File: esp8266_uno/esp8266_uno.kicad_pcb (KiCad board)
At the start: 2 copper layers, 69 x 53.9 mm, 131 parts, among them J1 Barrel_Jack, P1 USB, Q1 2N2222, Q2 2N2222, SW1 RESET, U1 ESP-12, U2 AMS1117-3.3, U3 CH340G, U4 ESP-13-WROOM-02, X1 12MHz

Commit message: added esp8266 in arduino uno format - hw design 5th pass
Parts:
- removed V13_13, V13_14, V14_11, V14_12, V14_13, V14_9, V15_10, V15_2, V17_5, V5_10, V5_11, V5_12, V6_4, V6_5, V7_10, V7_11: AUTO_VIA, VIA_MATRIX
- added D1: SS34, w_smd_diode:do214ab, F.Cu at (126.0, 117.0)
- added V10_11: AUTO_VIA, VIA_MATRIX, F.Cu at (141.9, 118.7)
- added V11_13: AUTO_VIA, VIA_MATRIX, F.Cu at (145.7, 126.3)
- added V18_1: AUTO_VIA, VIA_MATRIX, F.Cu at (172.4, 80.6)
- added V18_3: AUTO_VIA, VIA_MATRIX, F.Cu at (172.4, 88.2)
- added V18_4: AUTO_VIA, VIA_MATRIX, F.Cu at (172.4, 92.0)
- added V18_8: AUTO_VIA, VIA_MATRIX, F.Cu at (172.4, 107.3)
- added V18_9: AUTO_VIA, VIA_MATRIX, F.Cu at (172.4, 111.1)
- added V3_7: AUTO_VIA, VIA_MATRIX, F.Cu at (115.2, 103.5)
- added V5_1: AUTO_VIA, VIA_MATRIX, F.Cu at (122.9, 80.6)
- added V6_12: AUTO_VIA, VIA_MATRIX, F.Cu at (126.7, 122.5)
- added V9_12: AUTO_VIA, VIA_MATRIX, F.Cu at (138.1, 122.5)
- U1: footprint ESP-12 -> myfootprints:ESP-12
- moved V13_12 0.88 mm to (153.3, 122.5)
- moved V17_3 0.86 mm to (168.6, 88.2)
- moved V13_11 0.85 mm to (153.3, 118.7)
- moved V12_12 0.85 mm to (149.5, 122.5)
- moved V13_10 0.82 mm to (153.3, 114.9)
- moved V12_11 0.81 mm to (149.5, 118.7)
- moved V16_3 0.81 mm to (164.8, 88.2)
- moved V8_14 0.81 mm to (134.3, 130.1)
- moved V13_9 0.79 mm to (153.3, 111.1)
- moved V9_13 0.79 mm to (138.1, 126.3)
- moved V7_14 0.78 mm to (130.5, 130.1)
- moved V10_12 0.78 mm to (141.9, 122.5)
- moved V12_10 0.78 mm to (149.5, 114.9)
- moved V11_11 0.78 mm to (145.7, 118.7)
- moved V8_13 0.76 mm to (134.3, 126.3)
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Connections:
- A1 pad 1: Net-(A1-Pad1) -> (no net)
- A1 pad 10: Net-(A1-Pad10) -> (no net)
- A1 pad 11: Net-(A1-Pad11) -> (no net)
- A1 pad 12: Net-(A1-Pad12) -> (no net)
- A1 pad 2: Net-(A1-Pad2) -> (no net)
- A1 pad 24: Net-(A1-Pad24) -> (no net)
- A1 pad 25: Net-(A1-Pad25) -> (no net)
- A1 pad 26: Net-(A1-Pad26) -> (no net)
- A1 pad 27: Net-(A1-Pad27) -> (no net)
- A1 pad 28: Net-(A1-Pad28) -> (no net)
- A1 pad 30: Net-(A1-Pad30) -> (no net)
- A1 pad 8: Net-(A1-Pad8) -> (no net)
- J1 pad 1: +5V -> Net-(D1-Pad2)
- U3 pad 10: Net-(U3-Pad10) -> (no net)
- U3 pad 11: Net-(U3-Pad11) -> (no net)
- U3 pad 12: Net-(U3-Pad12) -> (no net)
- U3 pad 15: Net-(U3-Pad15) -> (no net)
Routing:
- net +5V: track 77.7 -> 68.6 mm
- net Net-(D1-Pad2): track 0.00 -> 8.39 mm

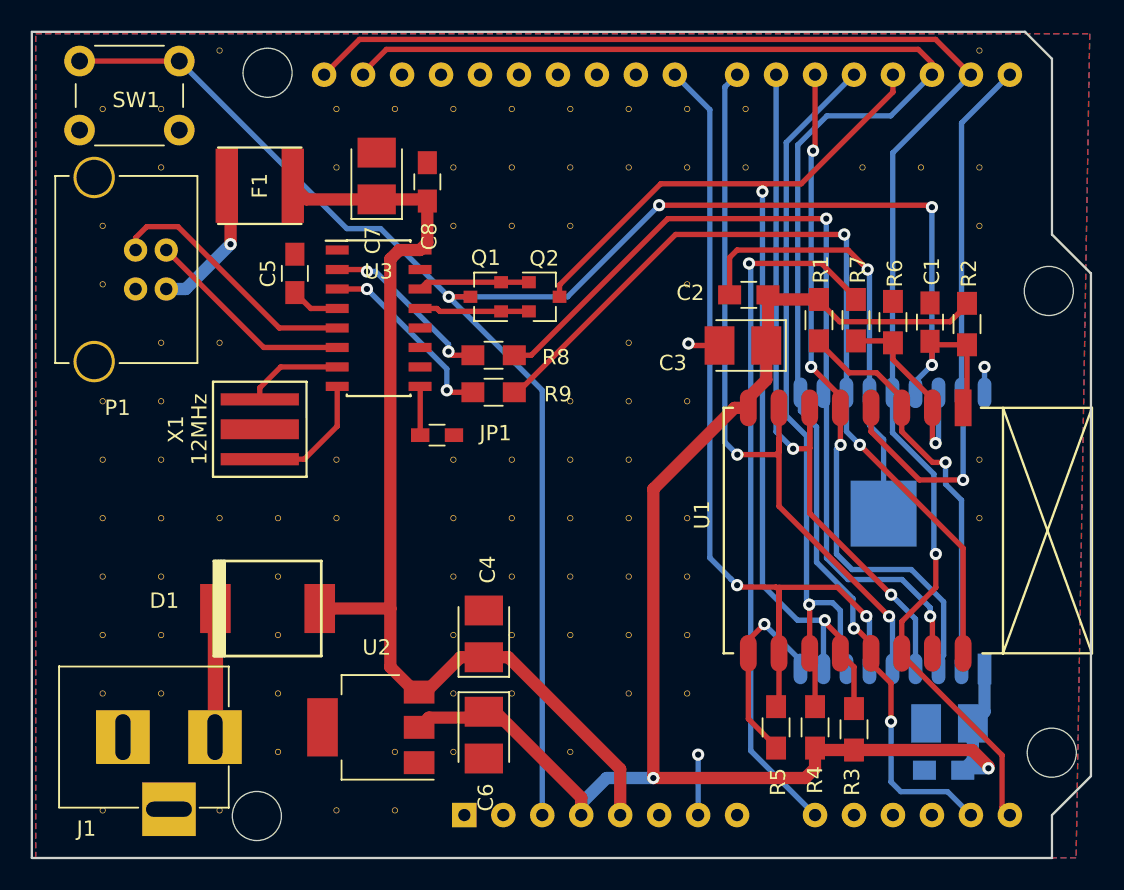
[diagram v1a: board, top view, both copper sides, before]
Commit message: added esp8266 in arduino uno format - hw design 6th pass
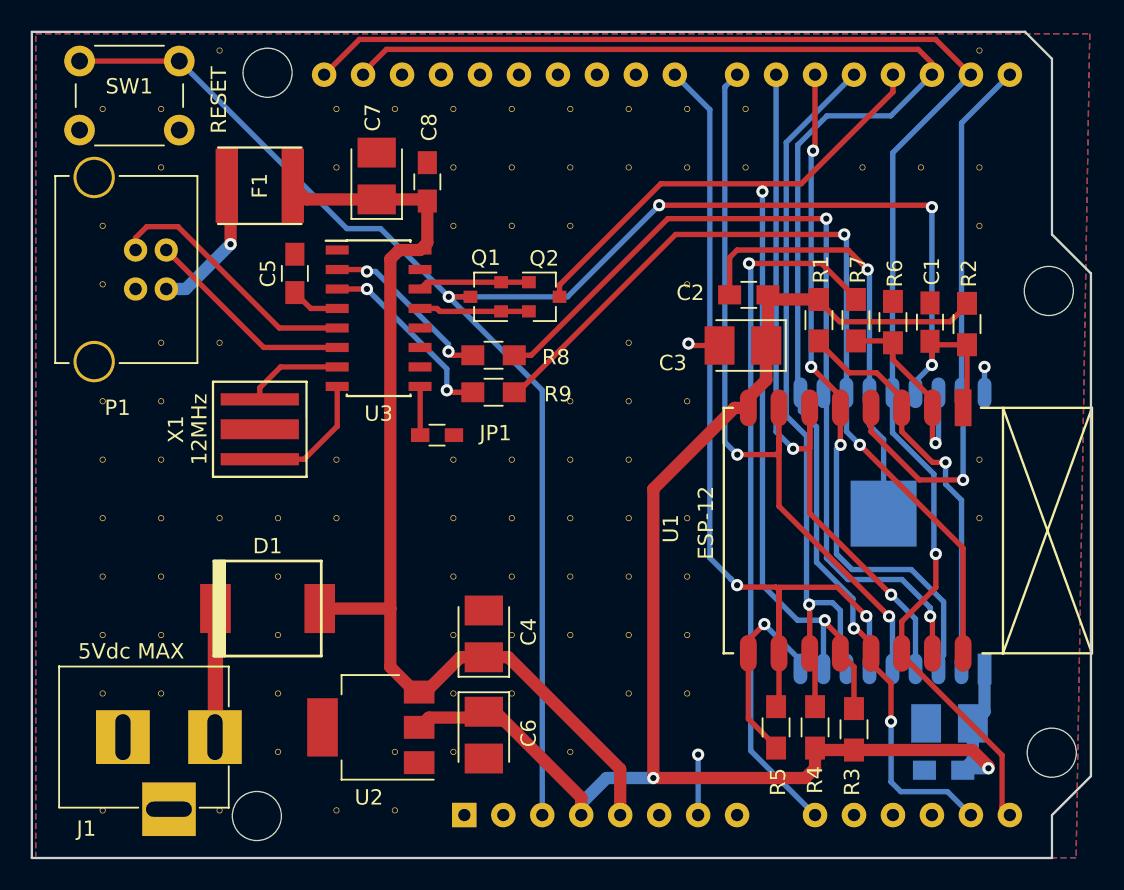
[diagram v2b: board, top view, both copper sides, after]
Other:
- board text added: "5Vdc MAX"

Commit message: added esp8266 in arduino uno format - hw design 7th pass
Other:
- board text added: "REV 0.2"
- board text removed: "REV 0.1"
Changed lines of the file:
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@@
   )
   (gr_line (start 177.1142 81.1276) (end 175.3616 79.375) (layer Edge.Cuts) (width 0.15))
-  (gr_text "REV 0.1" (at 144.399 92.837) (layer B.SilkS)
+  (gr_text "REV 0.2" (at 144.399 92.837) (layer B.SilkS)
     (effects (font (size 1.5 1.5) (thickness 0.3)) (justify mirror))
   )

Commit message: added esp8266 in arduino uno format - hw design final pass
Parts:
- removed V5_14: AUTO_VIA, VIA_MATRIX
- moved REF** 1.30 mm to (177.2, 97.5)
- moved REF** 0.91 mm to (177.3, 125.5)
- moved REF** 0.46 mm to (126.4, 82.3)
- moved REF** 0.20 mm to (125.1, 130.4)
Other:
- board size 69 x 53.9 mm -> 68.5 x 53.5 mm
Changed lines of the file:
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@@
   (general
     (thickness 1.6)
-    (drawings 11)
+    (drawings 56)
     (tracks 376)
     (zones 0)
-    (modules 127)
+    (modules 126)
     (nets 31)
   )
@@
     (38 B.Mask user)
     (39 F.Mask user)
-    (40 Dwgs.User user)
+    (40 Dwgs.User user hide)
     (41 Cmts.User user hide)
     (42 Eco1.User user hide)
@@
   )
   (module Mounting_Holes:MountingHole_3.2mm_M3 locked (layer F.Cu)
-    (at 125.2855 130.4925)
+    (at 125.095 130.429)
     (descr "Mounting Hole 3.2mm, no annular, M3")
     (tags "mounting hole 3.2mm no annular m3")
@@
   )
   (module Mounting_Holes:MountingHole_3.2mm_M3 locked (layer F.Cu)
-    (at 125.984 82.042)
+    (at 126.365 82.296)
     (descr "Mounting Hole 3.2mm, no annular, M3")
     (tags "mounting hole 3.2mm no annular m3")
@@
   )
   (module Mounting_Holes:MountingHole_3.2mm_M3 locked (layer F.Cu)
-    (at 176.911 96.266)
+    (at 177.165 97.536)
     (descr "Mounting Hole 3.2mm, no annular, M3")
     (tags "mounting hole 3.2mm no annular m3")
@@
   )
   (module Mounting_Holes:MountingHole_3.2mm_M3 locked (layer F.Cu)
-    (at 177.1015 126.365)
+    (at 177.292 125.476)
     (descr "Mounting Hole 3.2mm, no annular, M3")
     (tags "mounting hole 3.2mm no annular m3")
@@
   )
   (module VIA_MATRIX (layer F.Cu)
-    (at 122.854999 130.1245)
-    (attr virtual)
-    (fp_text reference V5_14 (at 0 0) (layer F.SilkS) hide
-      (effects (font (size 0 0) (thickness 0.15)))
-    )
-    (fp_text value AUTO_VIA (at 0 0) (layer F.Fab) hide
-      (effects (font (size 0 0) (thickness 0.15)))
-    )
-    (pad 1 thru_hole circle (at 0 0) (size 0.4 0.4) (drill 0.3) (layers *.Cu)
-      (net 3 GND) (clearance 0.3) (zone_connect 2))
-  )
-  (module VIA_MATRIX (layer F.Cu)
     (at 130.474999 130.1245)
     (attr virtual)
@@
       (net 3 GND) (clearance 0.3) (zone_connect 2))
   )
+  (gr_circle (center 140.111 82.296) (end 140.365 82.296) (layer Dwgs.User) (width 0.2))
+  (gr_circle (center 142.651 82.296) (end 142.905 82.296) (layer Dwgs.User) (width 0.2))
+  (gr_circle (center 145.191 82.296) (end 145.445 82.296) (layer Dwgs.User) (width 0.2))
+  (gr_circle (center 172.085 82.296) (end 172.339 82.296) (layer Dwgs.User) (width 0.2))
+  (gr_circle (center 174.625 82.296) (end 174.879 82.296) (layer Dwgs.User) (width 0.2))
+  (gr_circle (center 139.065 130.556) (end 139.319 130.556) (layer Dwgs.User) (width 0.2))
+  (gr_circle (center 177.195 97.536) (end 178.7825 97.536) (layer Dwgs.User) (width 0.2))
+  (gr_circle (center 126.395 82.296) (end 127.9825 82.296) (layer Dwgs.User) (width 0.2))
+  (gr_line (start 177.195 81.282319) (end 177.195 92.71) (layer Dwgs.User) (width 0.2))
+  (gr_line (start 177.195 133.096) (end 111.125 133.096) (layer Dwgs.User) (width 0.2))
+  (gr_line (start 179.675 95.25) (end 179.675 128.016) (layer Dwgs.User) (width 0.2))
+  (gr_circle (center 129.951 82.296) (end 130.205 82.296) (layer Dwgs.User) (width 0.2))
+  (gr_circle (center 174.625 130.556) (end 174.879 130.556) (layer Dwgs.User) (width 0.2))
+  (gr_circle (center 125.095 130.556) (end 126.6825 130.556) (layer Dwgs.User) (width 0.2))
+  (gr_circle (center 177.195 125.476) (end 178.7825 125.476) (layer Dwgs.User) (width 0.2))
+  (gr_line (start 177.195 81.282319) (end 175.630208 79.717527) (layer Dwgs.User) (width 0.2))
+  (gr_line (start 175.630208 79.717527) (end 111.125 79.717527) (layer Dwgs.User) (width 0.2))
+  (gr_line (start 111.125 133.096) (end 111.125 79.717527) (layer Dwgs.User) (width 0.2))
+  (gr_line (start 179.675 128.016) (end 177.195 130.556) (layer Dwgs.User) (width 0.2))
+  (gr_line (start 177.195 92.71) (end 179.675 95.25) (layer Dwgs.User) (width 0.2))
+  (gr_line (start 177.195 133.096) (end 177.195 130.556) (layer Dwgs.User) (width 0.2))
+  (gr_circle (center 167.005 130.556) (end 167.259 130.556) (layer Dwgs.User) (width 0.2))
+  (gr_circle (center 169.545 130.556) (end 169.799 130.556) (layer Dwgs.User) (width 0.2))
+  (gr_circle (center 172.085 130.556) (end 172.339 130.556) (layer Dwgs.User) (width 0.2))
+  (gr_circle (center 164.465 82.296) (end 164.719 82.296) (layer Dwgs.User) (width 0.2))
+  (gr_circle (center 167.005 82.296) (end 167.259 82.296) (layer Dwgs.User) (width 0.2))
+  (gr_circle (center 169.545 82.296) (end 169.799 82.296) (layer Dwgs.User) (width 0.2))
+  (gr_circle (center 147.731 82.296) (end 147.985 82.296) (layer Dwgs.User) (width 0.2))
+  (gr_circle (center 150.271 82.296) (end 150.525 82.296) (layer Dwgs.User) (width 0.2))
+  (gr_circle (center 152.811 82.296) (end 153.065 82.296) (layer Dwgs.User) (width 0.2))
+  (gr_circle (center 156.845 82.296) (end 157.099 82.296) (layer Dwgs.User) (width 0.2))
+  (gr_circle (center 159.385 82.296) (end 159.639 82.296) (layer Dwgs.User) (width 0.2))
+  (gr_circle (center 161.925 82.296) (end 162.179 82.296) (layer Dwgs.User) (width 0.2))
+  (gr_circle (center 156.845 130.556) (end 157.099 130.556) (layer Dwgs.User) (width 0.2))
+  (gr_circle (center 161.925 130.556) (end 162.179 130.556) (layer Dwgs.User) (width 0.2))
+  (gr_circle (center 164.465 130.556) (end 164.719 130.556) (layer Dwgs.User) (width 0.2))
+  (gr_circle (center 149.225 130.556) (end 149.479 130.556) (layer Dwgs.User) (width 0.2))
+  (gr_circle (center 151.765 130.556) (end 152.019 130.556) (layer Dwgs.User) (width 0.2))
+  (gr_circle (center 154.305 130.556) (end 154.559 130.556) (layer Dwgs.User) (width 0.2))
+  (gr_circle (center 132.491 82.296) (end 132.745 82.296) (layer Dwgs.User) (width 0.2))
+  (gr_circle (center 135.031 82.296) (end 135.285 82.296) (layer Dwgs.User) (width 0.2))
+  (gr_circle (center 137.571 82.296) (end 137.825 82.296) (layer Dwgs.User) (width 0.2))
+  (gr_circle (center 141.605 130.556) (end 141.859 130.556) (layer Dwgs.User) (width 0.2))
+  (gr_circle (center 144.145 130.556) (end 144.399 130.556) (layer Dwgs.User) (width 0.2))
+  (gr_circle (center 146.685 130.556) (end 146.939 130.556) (layer Dwgs.User) (width 0.2))
   (gr_text "5Vdc MAX" (at 117.094 119.761) (layer F.SilkS)
     (effects (font (size 1 1) (thickness 0.15)))
   )
-  (gr_line (start 177.1142 81.1276) (end 175.3616 79.375) (layer Edge.Cuts) (width 0.15))
+  (gr_line (start 177.1142 81.1276) (end 175.7426 79.756) (layer Edge.Cuts) (width 0.15))
   (gr_text "REV 0.2" (at 144.399 92.837) (layer B.SilkS)
     (effects (font (size 1.5 1.5) (thickness 0.3)) (justify mirror))
   )
-  (gr_line (start 110.617 79.375) (end 110.617 133.223) (layer Edge.Cuts) (width 0.15))
-  (gr_line (start 175.3616 79.375) (end 110.617 79.375) (layer Edge.Cuts) (width 0.15))
+  (gr_line (start 111.125 79.756) (end 111.125 133.223) (layer Edge.Cuts) (width 0.15))
+  (gr_line (start 175.7426 79.756) (end 111.125 79.756) (layer Edge.Cuts) (width 0.15))
   (gr_line (start 177.115604 92.583266) (end 177.115604 81.127494) (layer Edge.Cuts) (width 0.15))
   (gr_line (start 179.655604 95.122997) (end 177.115604 92.582997) (layer Edge.Cuts) (width 0.15))
@@
   (gr_line (start 177.115604 130.435174) (end 179.655604 127.895174) (layer Edge.Cuts) (width 0.15))
   (gr_line (start 177.115604 133.229174) (end 177.115604 130.435174) (layer Edge.Cuts) (width 0.15))
-  (gr_line (start 110.617 133.229174) (end 177.115604 133.229174) (layer Edge.Cuts) (width 0.15))
+  (gr_line (start 111.125 133.229174) (end 177.115604 133.229174) (layer Edge.Cuts) (width 0.15))
   (segment (start 166.72 102.904) (end 166.72 105.506) (width 0.35) (layer B.Cu) (net 1) (status 10))
   (segment (start 166.72 105.506) (end 169.418 108.204) (width 0.35) (layer B.Cu) (net 1))
